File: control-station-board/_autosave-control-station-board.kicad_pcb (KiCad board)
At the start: 2 copper layers, 9.7 x 10.3 mm, 41 parts, among them J1 USB_B, J2 USB_B, J3 CAM1_OUT, J4 CAM2_OUT, U1 MAX4445, U2 LTC1983ES6-5-TRPBF, U3 MAX4445, U4 THVD1550DR, U5 FT232RL, U6 ATA6560,1, U7 FT232RL

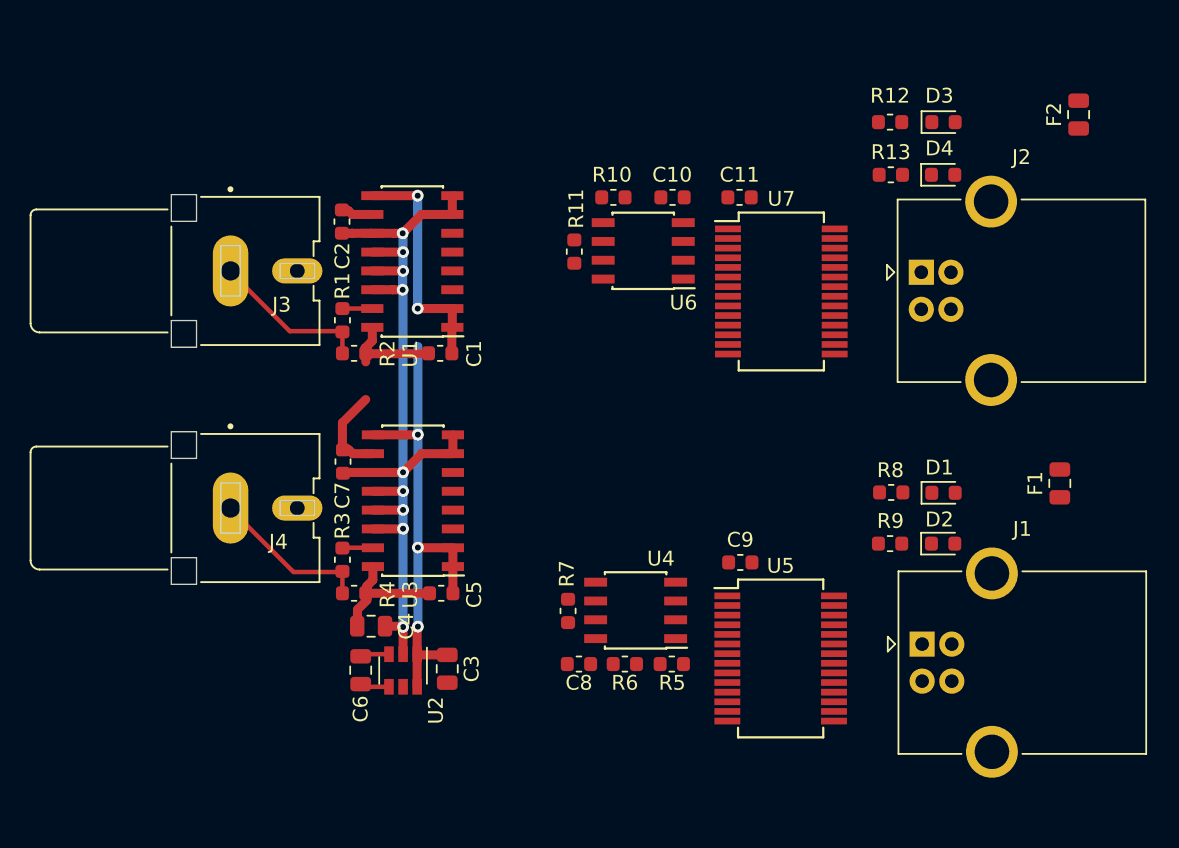
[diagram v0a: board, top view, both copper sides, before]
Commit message: Adding full deplex rs485
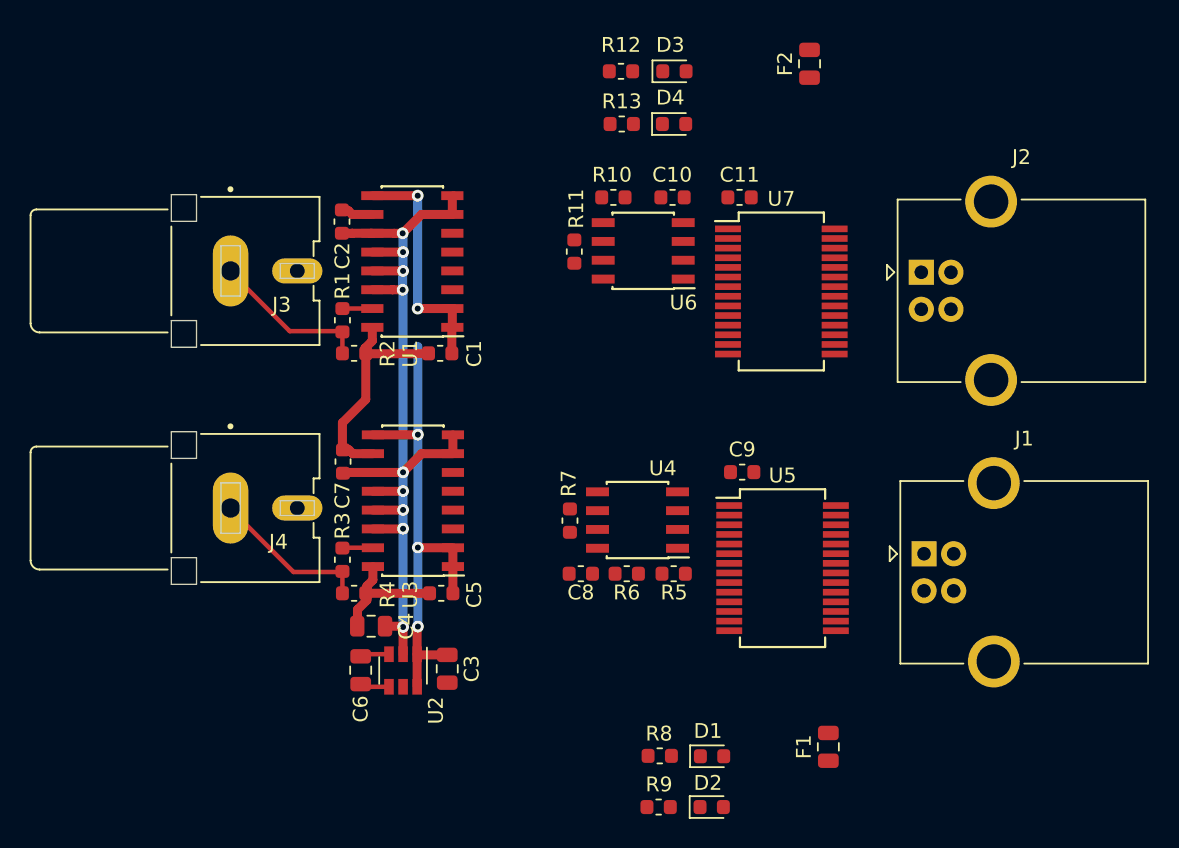
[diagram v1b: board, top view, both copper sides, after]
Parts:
- moved D2 23.7 mm to (68.3, 116.5)
- moved D1 23.7 mm to (68.3, 113.0)
- moved F1 23.7 mm to (76.2, 112.4)
- moved R8 23.7 mm to (64.8, 113.0)
- moved R9 23.7 mm to (64.7, 116.5)
- moved D3 18.5 mm to (65.8, 66.8)
- moved D4 18.5 mm to (65.8, 70.4)
- moved F2 18.5 mm to (74.9, 66.3)
- moved R12 18.5 mm to (62.2, 66.8)
- moved R13 18.5 mm to (62.3, 70.4)
- moved C8 6.10 mm to (59.5, 100.7)
- moved J1 6.10 mm to (82.7, 99.4)
- moved R5 6.10 mm to (65.8, 100.7)
- moved R6 6.10 mm to (62.6, 100.7)
- moved R7 6.10 mm to (58.8, 97.1)
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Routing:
- net GND: track 24.3 -> 26.8 mm
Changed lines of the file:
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@@
   )
   (module Fuse:Fuse_0805_2012Metric (layer F.Cu)
-    (at 91.817729 94.614663 90)
+    (at 76.196729 112.394663 90)
     (descr "Fuse SMD 0805 (2012 Metric), square (rectangular) end terminal, IPC_7351 nominal, (Body size source: https://docs.google.com/spreadsheets/d/1BsfQQcO9C6DZCsRaXUlFlo91Tg2WpOkGARC1WS5S8t0/edit?usp=sharing), generated with kicad-footprint-generator")
     (tags resistor)
@@
   )
   (module Fuse:Fuse_0805_2012Metric (layer F.Cu)
-    (at 93.087729 69.722663 90)
+    (at 74.926729 66.293663 90)
     (descr "Fuse SMD 0805 (2012 Metric), square (rectangular) end terminal, IPC_7351 nominal, (Body size source: https://docs.google.com/spreadsheets/d/1BsfQQcO9C6DZCsRaXUlFlo91Tg2WpOkGARC1WS5S8t0/edit?usp=sharing), generated with kicad-footprint-generator")
     (tags resistor)
@@
   )
   (module Capacitor_SMD:C_0603_1608Metric (layer F.Cu)
-    (at 70.253229 99.948663)
+    (at 70.380229 93.852663)
     (descr "Capacitor SMD 0603 (1608 Metric), square (rectangular) end terminal, IPC_7351 nominal, (Body size source: http://www.tortai-tech.com/upload/download/2011102023233369053.pdf), generated with kicad-footprint-generator")
     (tags capacitor)
@@
   )
   (module Capacitor_SMD:C_0603_1608Metric (layer F.Cu)
-    (at 59.364198 106.806663)
+    (at 59.491198 100.710663)
     (descr "Capacitor SMD 0603 (1608 Metric), square (rectangular) end terminal, IPC_7351 nominal, (Body size source: http://www.tortai-tech.com/upload/download/2011102023233369053.pdf), generated with kicad-footprint-generator")
     (tags capacitor)
@@
   )
   (module Connector_USB:USB_B_OST_USB-B1HSxx_Horizontal (layer F.Cu)
-    (at 82.527929 105.460463)
+    (at 82.654929 99.364463)
     (descr "USB B receptacle, Horizontal, through-hole, http://www.on-shore.com/wp-content/uploads/2015/09/usb-b1hsxx.pdf")
     (tags "USB-B receptacle horizontal through-hole")
@@
   )
   (module LED_SMD:LED_0603_1608Metric (layer F.Cu)
-    (at 83.969229 95.249663)
+    (at 68.348229 113.029663)
     (descr "LED SMD 0603 (1608 Metric), square (rectangular) end terminal, IPC_7351 nominal, (Body size source: http://www.tortai-tech.com/upload/download/2011102023233369053.pdf), generated with kicad-footprint-generator")
     (tags diode)
@@
   )
   (module LED_SMD:LED_0603_1608Metric (layer F.Cu)
-    (at 83.943729 98.678663)
+    (at 68.322729 116.458663)
     (descr "LED SMD 0603 (1608 Metric), square (rectangular) end terminal, IPC_7351 nominal, (Body size source: http://www.tortai-tech.com/upload/download/2011102023233369053.pdf), generated with kicad-footprint-generator")
     (tags diode)
@@
   )
   (module LED_SMD:LED_0603_1608Metric (layer F.Cu)
-    (at 83.969229 70.230663)
+    (at 65.808229 66.801663)
     (descr "LED SMD 0603 (1608 Metric), square (rectangular) end terminal, IPC_7351 nominal, (Body size source: http://www.tortai-tech.com/upload/download/2011102023233369053.pdf), generated with kicad-footprint-generator")
     (tags diode)
@@
   )
   (module LED_SMD:LED_0603_1608Metric (layer F.Cu)
-    (at 83.943729 73.786663)
+    (at 65.782729 70.357663)
     (descr "LED SMD 0603 (1608 Metric), square (rectangular) end terminal, IPC_7351 nominal, (Body size source: http://www.tortai-tech.com/upload/download/2011102023233369053.pdf), generated with kicad-footprint-generator")
     (tags diode)
@@
   )
   (module Package_SO:SOIC-8_3.9x4.9mm_P1.27mm (layer F.Cu)
-    (at 63.189073 103.184277 180)
+    (at 63.316073 97.088277 180)
     (descr "8-Lead Plastic Small Outline (SN) - Narrow, 3.90 mm Body [SOIC] (see Microchip Packaging Specification 00000049BS.pdf)")
     (tags "SOIC 1.27")
@@
   )
   (module Package_SO:SSOP-28_5.3x10.2mm_P0.65mm (layer F.Cu)
-    (at 72.977729 106.429663)
+    (at 73.104729 100.333663)
     (descr "28-Lead Plastic Shrink Small Outline (SS)-5.30 mm Body [SSOP] (see Microchip Packaging Specification 00000049BS.pdf)")
     (tags "SSOP 0.65")
@@
   )
   (module Resistor_SMD:R_0603_1608Metric (layer F.Cu)
-    (at 80.413229 73.786663 180)
+    (at 62.252229 70.357663 180)
     (descr "Resistor SMD 0603 (1608 Metric), square (rectangular) end terminal, IPC_7351 nominal, (Body size source: http://www.tortai-tech.com/upload/download/2011102023233369053.pdf), generated with kicad-footprint-generator")
     (tags resistor)
@@
   )
   (module Resistor_SMD:R_0603_1608Metric (layer F.Cu)
-    (at 65.630229 106.806663)
+    (at 65.757229 100.710663)
     (descr "Resistor SMD 0603 (1608 Metric), square (rectangular) end terminal, IPC_7351 nominal, (Body size source: http://www.tortai-tech.com/upload/download/2011102023233369053.pdf), generated with kicad-footprint-generator")
     (tags resistor)
@@
   )
   (module Resistor_SMD:R_0603_1608Metric (layer F.Cu)
-    (at 62.463198 106.806663)
+    (at 62.590198 100.710663)
     (descr "Resistor SMD 0603 (1608 Metric), square (rectangular) end terminal, IPC_7351 nominal, (Body size source: http://www.tortai-tech.com/upload/download/2011102023233369053.pdf), generated with kicad-footprint-generator")
     (tags resistor)
@@
   )
   (module Resistor_SMD:R_0603_1608Metric (layer F.Cu)
-    (at 58.627698 103.222323 90)
+    (at 58.754698 97.126323 90)
     (descr "Resistor SMD 0603 (1608 Metric), square (rectangular) end terminal, IPC_7351 nominal, (Body size source: http://www.tortai-tech.com/upload/download/2011102023233369053.pdf), generated with kicad-footprint-generator")
     (tags resistor)
@@
   )
   (module Resistor_SMD:R_0603_1608Metric (layer F.Cu)
-    (at 80.438429 95.224263 180)
+    (at 64.817429 113.004263 180)
     (descr "Resistor SMD 0603 (1608 Metric), square (rectangular) end terminal, IPC_7351 nominal, (Body size source: http://www.tortai-tech.com/upload/download/2011102023233369053.pdf), generated with kicad-footprint-generator")
     (tags resistor)
@@
   )
   (module Resistor_SMD:R_0603_1608Metric (layer F.Cu)
-    (at 80.362229 70.230663 180)
+    (at 62.201229 66.801663 180)
     (descr "Resistor SMD 0603 (1608 Metric), square (rectangular) end terminal, IPC_7351 nominal, (Body size source: http://www.tortai-tech.com/upload/download/2011102023233369053.pdf), generated with kicad-footprint-generator")
     (tags resistor)
@@
   )
   (module Resistor_SMD:R_0603_1608Metric (layer F.Cu)
-    (at 80.362229 98.678663 180)
+    (at 64.741229 116.458663 180)
     (descr "Resistor SMD 0603 (1608 Metric), square (rectangular) end terminal, IPC_7351 nominal, (Body size source: http://www.tortai-tech.com/upload/download/2011102023233369053.pdf), generated with kicad-footprint-generator")
     (tags resistor)
@@
     )
   )
-  (segment (start 44.096807 92.607185) (end 43.829573 92.339951) (width 0.6096) (layer F.Cu) (net 3))
-  (segment (start 45.456407 92.607185) (end 44.096807 92.607185) (width 0.6096) (layer F.Cu) (net 3))
-  (segment (start 43.829573 92.339951) (end 43.400647 92.339951) (width 0.6096) (layer F.Cu) (net 3))
   (segment (start 44.058505 76.462907) (end 43.806549 76.210951) (width 0.6096) (layer F.Cu) (net 3))
   (segment (start 45.418105 76.462907) (end 44.058505 76.462907) (width 0.6096) (layer F.Cu) (net 3))
@@
   (segment (start 49.210305 85.835507) (end 49.143091 85.835507) (width 0.6096) (layer F.Cu) (net 3))
   (segment (start 49.143091 85.835507) (end 49.115647 85.862951) (width 0.6096) (layer F.Cu) (net 3))
+  (segment (start 44.096807 92.607185) (end 45.456407 92.607185) (width 0.6096) (layer F.Cu) (net 3))
+  (segment (start 43.829573 92.339951) (end 44.096807 92.607185) (width 0.6096) (layer F.Cu) (net 3))
+  (segment (start 43.400647 92.339951) (end 43.829573 92.339951) (width 0.6096) (layer F.Cu) (net 3))
+  (segment (start 43.400647 90.525507) (end 43.400647 92.339951) (width 0.6096) (layer F.Cu) (net 3))
+  (segment (start 44.975647 85.835507) (end 44.975647 88.950507) (width 0.6096) (layer F.Cu) (net 3))
   (segment (start 44.975647 88.950507) (end 43.400647 90.525507) (width 0.6096) (layer F.Cu) (net 3))
-  (segment (start 44.975647 85.835507) (end 44.975647 86.410507) (width 0.6096) (layer F.Cu) (net 3))
-  (segment (start 43.400647 90.525507) (end 43.400647 92.339951) (width 0.6096) (layer F.Cu) (net 3))
   (segment (start 43.400647 102.030585) (end 43.400647 100.594951) (width 0.3048) (layer F.Cu) (net 4))
   (segment (start 43.400647 100.594951) (end 40.098647 100.594951) (width 0.3048) (layer F.Cu) (net 4))
